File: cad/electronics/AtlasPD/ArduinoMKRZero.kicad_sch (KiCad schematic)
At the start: 1 part, among them U500 Arduino_MKR_Zero

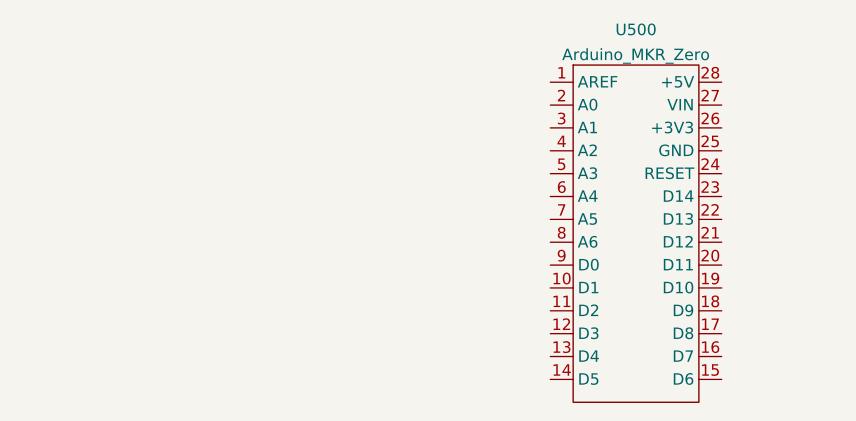
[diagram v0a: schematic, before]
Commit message: Eliminated need for AND gate IC
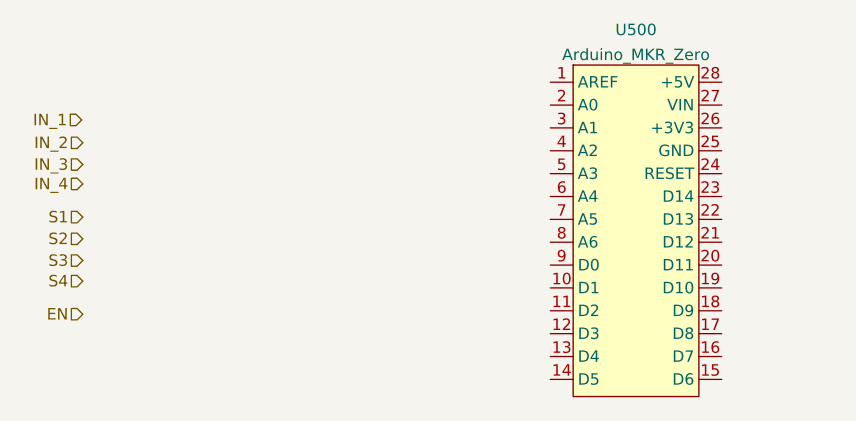
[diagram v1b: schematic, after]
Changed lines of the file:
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@@
 (kicad_sch (version 20211123) (generator eeschema)
   (paper "A4")
+  (hierarchical_label "IN_3" (shape input) (at 28.448 54.483 180)
+    (effects (font (size 1.27 1.27)) (justify right))
+  )
+  (hierarchical_label "S1" (shape input) (at 28.448 60.325 180)
+    (effects (font (size 1.27 1.27)) (justify right))
+  )
+  (hierarchical_label "IN_4" (shape input) (at 28.448 56.642 180)
+    (effects (font (size 1.27 1.27)) (justify right))
+  )
+  (hierarchical_label "EN" (shape input) (at 28.448 71.12 180)
+    (effects (font (size 1.27 1.27)) (justify right))
+  )
+  (hierarchical_label "S3" (shape input) (at 28.448 65.151 180)
+    (effects (font (size 1.27 1.27)) (justify right))
+  )
+  (hierarchical_label "S2" (shape input) (at 28.448 62.738 180)
+    (effects (font (size 1.27 1.27)) (justify right))
+  )
+  (hierarchical_label "S4" (shape input) (at 28.448 67.437 180)
+    (effects (font (size 1.27 1.27)) (justify right))
+  )
+  (hierarchical_label "IN_1" (shape input) (at 28.321 49.53 180)
+    (effects (font (size 1.27 1.27)) (justify right))
+  )
+  (hierarchical_label "IN_2" (shape input) (at 28.448 52.07 180)
+    (effects (font (size 1.27 1.27)) (justify right))
+  )
   (symbol (lib_id "SamacSys_Parts:Arduino_MKR_Zero") (at 89.916 52.324 0) (unit 1)
     (in_bom yes) (on_board yes) (fields_autoplaced)

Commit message: Layout updates for MKR
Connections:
- net EN: now also U500.14 (D5)
- net IN_1: now also U500.9 (D0)
- net IN_2: now also U500.10 (D1)
- net IN_3: now also U500.11 (D2)
- net IN_4: now also U500.12 (D3)
- net S1: now also U500.15 (D6)
- net S2: now also U500.16 (D7)
- net S3: now also U500.17 (D8)
- net S4: now also U500.18 (D9)
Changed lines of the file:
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@@
 (kicad_sch (version 20211123) (generator eeschema)
   (paper "A4")
-  (hierarchical_label "IN_3" (shape input) (at 28.448 54.483 180)
+  (wire (pts (xy 74.803 78.359) (xy 80.391 78.359))
+    (stroke (width 0) (type default) (color 0 0 0 0))
+  )
+  (wire (pts (xy 99.441 70.739) (xy 107.696 70.739))
+    (stroke (width 0) (type default) (color 0 0 0 0))
+  )
+  (wire (pts (xy 74.803 73.279) (xy 80.391 73.279))
+    (stroke (width 0) (type default) (color 0 0 0 0))
+  )
+  (wire (pts (xy 99.441 75.819) (xy 107.696 75.819))
+    (stroke (width 0) (type default) (color 0 0 0 0))
+  )
+  (wire (pts (xy 99.441 73.279) (xy 107.696 73.279))
+    (stroke (width 0) (type default) (color 0 0 0 0))
+  )
+  (wire (pts (xy 74.803 70.739) (xy 80.391 70.739))
+    (stroke (width 0) (type default) (color 0 0 0 0))
+  )
+  (wire (pts (xy 99.441 78.359) (xy 107.696 78.359))
+    (stroke (width 0) (type default) (color 0 0 0 0))
+  )
+  (wire (pts (xy 74.803 68.199) (xy 80.391 68.199))
+    (stroke (width 0) (type default) (color 0 0 0 0))
+  )
+  (wire (pts (xy 74.676 65.659) (xy 80.391 65.659))
+    (stroke (width 0) (type default) (color 0 0 0 0))
+  )
+  (hierarchical_label "IN_3" (shape input) (at 74.803 70.739 180)
     (effects (font (size 1.27 1.27)) (justify right))
   )
-  (hierarchical_label "S1" (shape input) (at 28.448 60.325 180)
+  (hierarchical_label "S1" (shape input) (at 107.696 78.359 0)
+    (effects (font (size 1.27 1.27)) (justify left))
+  )
+  (hierarchical_label "IN_4" (shape input) (at 74.803 73.279 180)
     (effects (font (size 1.27 1.27)) (justify right))
   )
-  (hierarchical_label "IN_4" (shape input) (at 28.448 56.642 180)
+  (hierarchical_label "EN" (shape input) (at 74.803 78.359 180)
     (effects (font (size 1.27 1.27)) (justify right))
   )
-  (hierarchical_label "EN" (shape input) (at 28.448 71.12 180)
+  (hierarchical_label "S3" (shape input) (at 107.696 73.279 0)
+    (effects (font (size 1.27 1.27)) (justify left))
+  )
+  (hierarchical_label "S2" (shape input) (at 107.696 75.819 0)
+    (effects (font (size 1.27 1.27)) (justify left))
+  )
+  (hierarchical_label "S4" (shape input) (at 107.696 70.739 0)
+    (effects (font (size 1.27 1.27)) (justify left))
+  )
+  (hierarchical_label "IN_1" (shape input) (at 74.676 65.659 180)
     (effects (font (size 1.27 1.27)) (justify right))
   )
-  (hierarchical_label "S3" (shape input) (at 28.448 65.151 180)
+  (hierarchical_label "IN_2" (shape input) (at 74.803 68.199 180)
     (effects (font (size 1.27 1.27)) (justify right))
   )
-  (hierarchical_label "S2" (shape input) (at 28.448 62.738 180)
-    (effects (font (size 1.27 1.27)) (justify right))
-  )
-  (hierarchical_label "S4" (shape input) (at 28.448 67.437 180)
-    (effects (font (size 1.27 1.27)) (justify right))
-  )
-  (hierarchical_label "IN_1" (shape input) (at 28.321 49.53 180)
-    (effects (font (size 1.27 1.27)) (justify right))
-  )
-  (hierarchical_label "IN_2" (shape input) (at 28.448 52.07 180)
-    (effects (font (size 1.27 1.27)) (justify right))
-  )
